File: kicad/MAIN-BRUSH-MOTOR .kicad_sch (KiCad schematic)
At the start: 6 parts, among them J11 MAIN BRUSH, Q10 AO3400

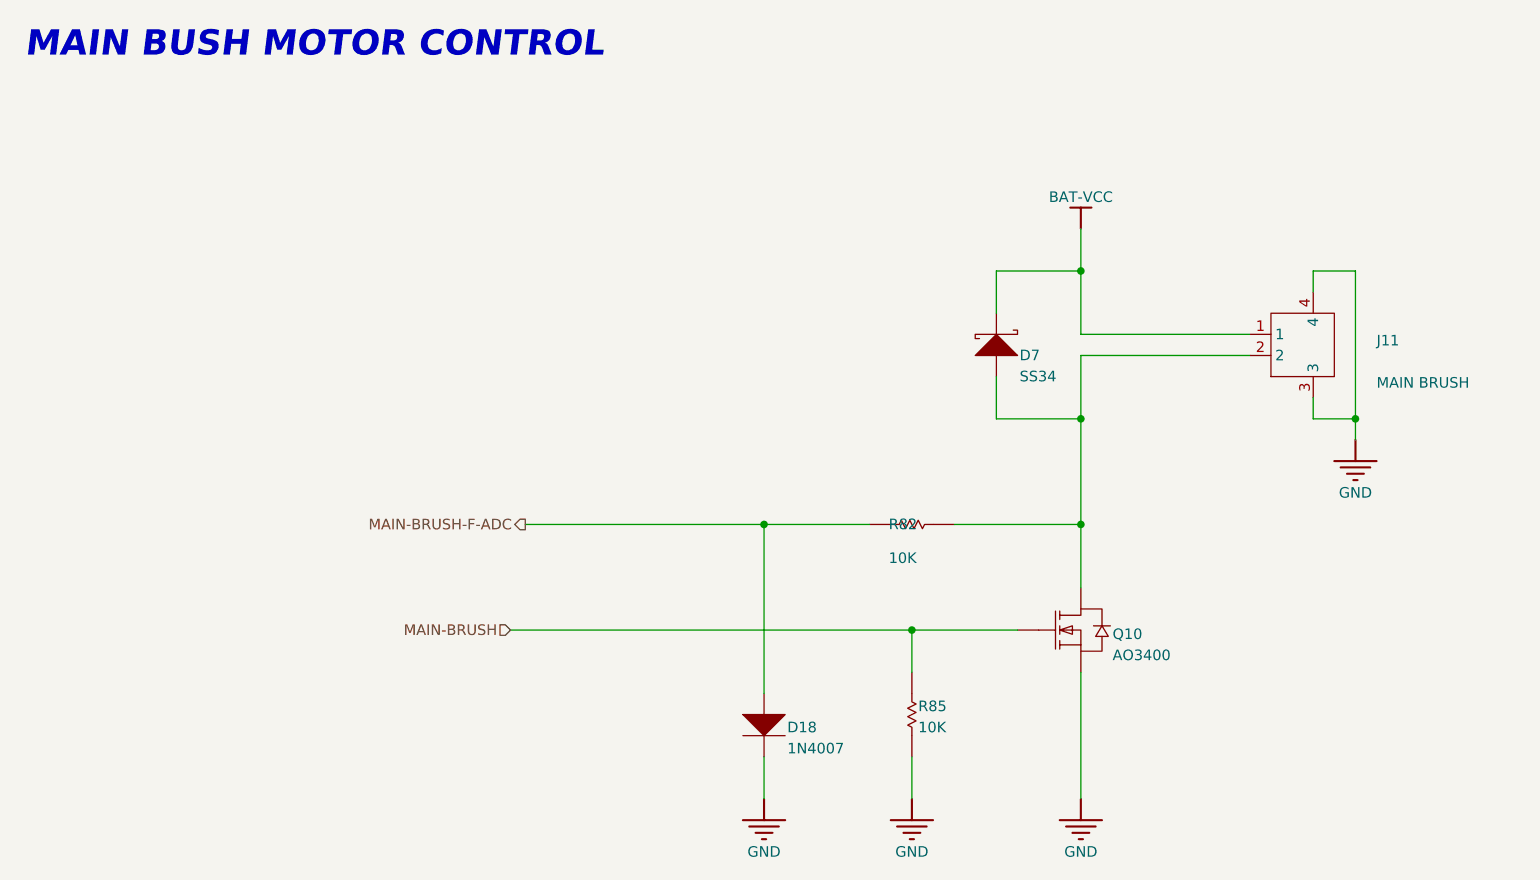
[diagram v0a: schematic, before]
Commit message: Changed MCU to STM32G473VCT6
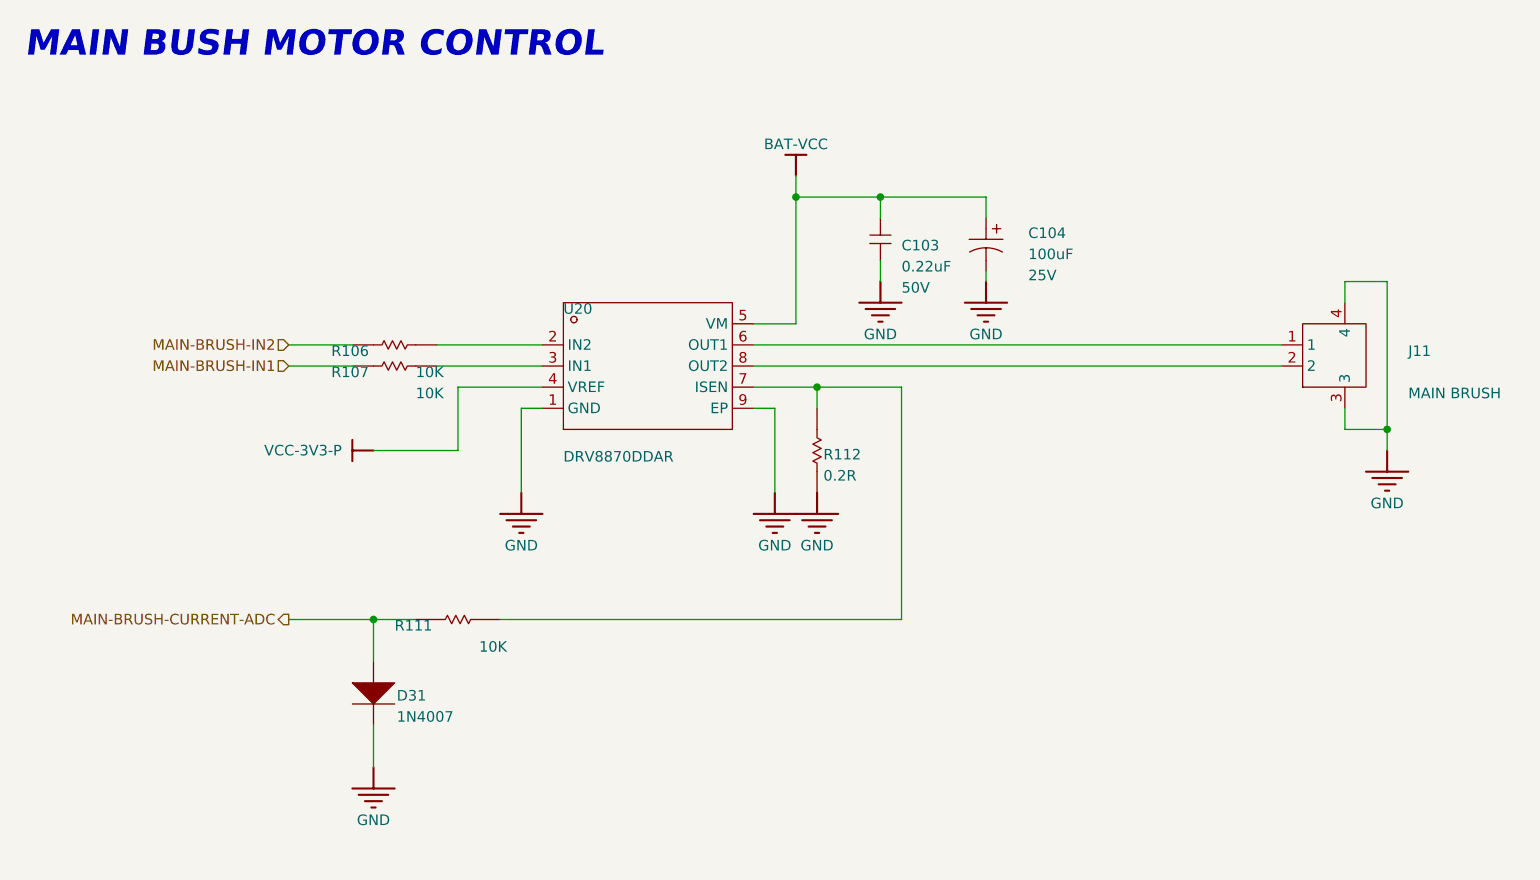
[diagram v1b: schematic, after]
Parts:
- removed D18: 1N4007, oomwoo_altium:SOD123, symbol DesignLibrary:MAIN-BRUSH MOTOR_3_DIODE-1_DesignLibrary.SchLib
- removed D7: SS34, oomwoo_altium:SMA, symbol DesignLibrary:MAIN-BRUSH MOTOR_1_DIODE-2_DesignLibrary.SchLib
- removed Q10: AO3400, oomwoo_altium:SOT23-3D, symbol DesignLibrary:MAIN-BRUSH MOTOR_0_N-MOS-SOT23_DesignLibrary.SchLib
- removed R82: 10K, oomwoo_altium:RES-0402, symbol DesignLibrary:MAIN-BRUSH MOTOR_0_Resistor-1_DesignLibrary.SchLib
- removed R85: 10K, oomwoo_altium:RES-0402, symbol DesignLibrary:MAIN-BRUSH MOTOR_3_Resistor-1_DesignLibrary.SchLib
- added C103: 0.22uF, Capacitor_SMD:C_0603_1608Metric, symbol DesignLibrary:WHEEL MOTOR_1_Capacitor-1_DesignLibrary.SchLib
- added C104: 100uF, oomwoo_altium:CAP-SMD_BD6.3-L6.6-W6.6-FD, symbol DesignLibrary:WHEEL MOTOR_3_Capacitor-2_DesignLibrary.SchLib
- added D31: 1N4007, oomwoo_altium:SOD123, symbol DesignLibrary:WHEEL MOTOR_3_DIODE-1_DesignLibrary.SchLib
- added R106, R107, R111: 10K, Resistor_SMD:R_0603_1608Metric, symbol DesignLibrary:WHEEL MOTOR_0_Resistor-1_DesignLibrary.SchLib
- added R112: 0.2R, Resistor_SMD:R_0603_1608Metric, symbol DesignLibrary:WHEEL MOTOR_1_Resistor-1_DesignLibrary.SchLib
- added U20: DRV8870DDAR, oomwoo_altium:HSOP-8_L5.0-W4.0-P1.27-LS6.2-BL-EP, symbol DesignLibrary:WHEEL MOTOR_0_DRV8870_DesignLibrary.SchLib
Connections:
- net BAT-VCC: now also C103.2, C104.1, U20.5 (VM); no longer J11.1
- net GND: now also C103.1, C104.2, D31.2 (K), R112.1, U20.1 (GND), U20.9 (EP)
- net at J11.2: now also U20.8 (OUT2)
- new net: R107.2, U20.3 (IN1)
- new net: J11.1, U20.6 (OUT1)
- new net: R111.2, R112.2, U20.7 (ISEN)
- new net: R106.2, U20.2 (IN2)
- new net MAIN-BRUSH-CURRENT-ADC: D31.1 (A), R111.1
- new net MAIN-BRUSH-IN1: R107.1
- new net MAIN-BRUSH-IN2: R106.1
- new net VCC-3V3-P: U20.4 (VREF)
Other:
- moved on the sheet: J11
